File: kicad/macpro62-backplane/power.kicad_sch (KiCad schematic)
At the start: 0 parts

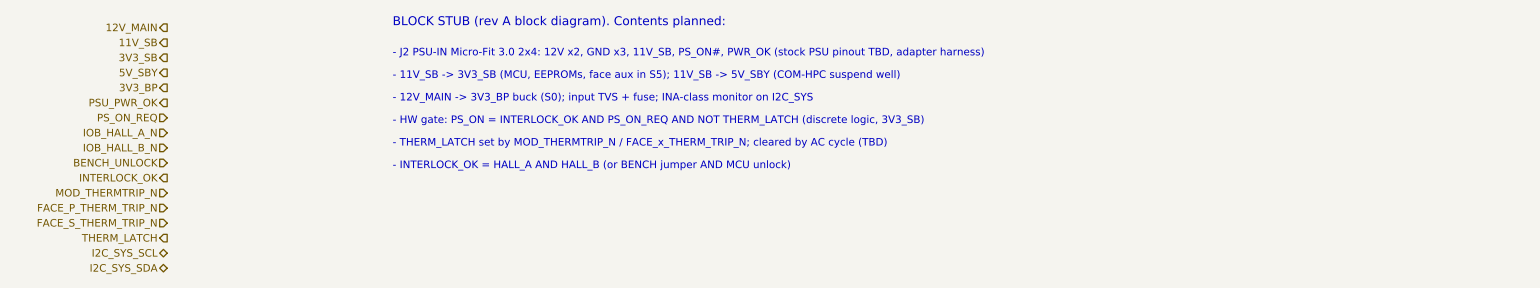
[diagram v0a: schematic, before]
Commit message: Cross-board compatibility audit: interface control doc, CR-BP-1 applied, J2/J3 row-swap pinouts, 15-pin face AUX, fan header removed from backplane, CPU board i226/BT1 cleanup
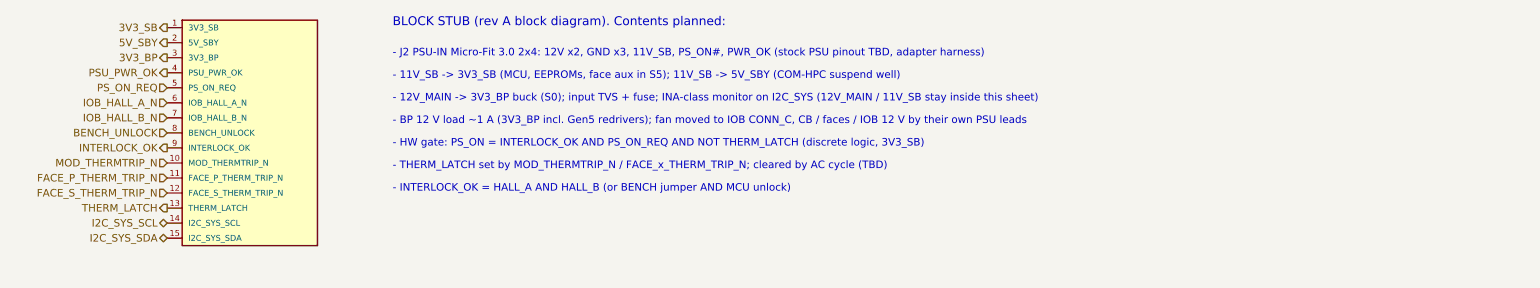
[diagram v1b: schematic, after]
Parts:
- added #BLK1: STUB_POWER, symbol MP62:STUB_POWER
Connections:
- net 3V3_BP: now also #BLK1.3 (3V3_BP)
- net 3V3_SB: now also #BLK1.1 (3V3_SB)
- net 5V_SBY: now also #BLK1.2 (5V_SBY)
- net BENCH_UNLOCK: now also #BLK1.8 (BENCH_UNLOCK)
- net FACE_P_THERM_TRIP_N: now also #BLK1.11 (FACE_P_THERM_TRIP_N)
- net FACE_S_THERM_TRIP_N: now also #BLK1.12 (FACE_S_THERM_TRIP_N)
- net I2C_SYS_SCL: now also #BLK1.14 (I2C_SYS_SCL)
- net I2C_SYS_SDA: now also #BLK1.15 (I2C_SYS_SDA)
- net INTERLOCK_OK: now also #BLK1.9 (INTERLOCK_OK)
- net IOB_HALL_A_N: now also #BLK1.6 (IOB_HALL_A_N)
- net IOB_HALL_B_N: now also #BLK1.7 (IOB_HALL_B_N)
- net MOD_THERMTRIP_N: now also #BLK1.10 (MOD_THERMTRIP_N)
- net PSU_PWR_OK: now also #BLK1.4 (PSU_PWR_OK)
- net PS_ON_REQ: now also #BLK1.5 (PS_ON_REQ)
- net THERM_LATCH: now also #BLK1.13 (THERM_LATCH)
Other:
- note added: "- 12V_MAIN -> 3V3_BP buck (S0); input TVS + fuse; INA-class monitor on I2C_SYS (12V_MAIN / 11V_SB stay inside this sheet)"
- note added: "- BP 12 V load ~1 A (3V3_BP incl. Gen5 redrivers); fan moved to IOB CONN_C, CB / faces / IOB 12 V by their own PSU leads"
- note removed: "- 12V_MAIN -> 3V3_BP buck (S0); input TVS + fuse; INA-class monitor on I2C_SYS"
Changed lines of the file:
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@@
 	(title_block
 		(title "MP62 backplane: Power input, standby rails, safety gate")
-		(date "2026-10-01")
-		(rev "A-bd1")
-		(comment 1 "Block stub: hierarchical labels only, circuit TBD")
+		(date "2026-10-02")
+		(rev "A-bd2")
+		(comment 1 "Block stub: hierarchical labels + one non-BOM stub symbol (#BLKn, passive pins) so ERC sees the nets; circuit TBD")
 	)
-	(hierarchical_label "12V_MAIN"
+	(hierarchical_label "3V3_SB"
 		(shape output)
 		(at 38.1 30.48 180)
 		(effects (font (size 1.27 1.27)) (justify right))
 	)
-	(hierarchical_label "11V_SB"
+	(hierarchical_label "5V_SBY"
 		(shape output)
 		(at 38.1 33.02 180)
 		(effects (font (size 1.27 1.27)) (justify right))
 	)
-	(hierarchical_label "3V3_SB"
+	(hierarchical_label "3V3_BP"
 		(shape output)
 		(at 38.1 35.56 180)
 		(effects (font (size 1.27 1.27)) (justify right))
 	)
-	(hierarchical_label "5V_SBY"
+	(hierarchical_label "PSU_PWR_OK"
 		(shape output)
 		(at 38.1 38.10 180)
 		(effects (font (size 1.27 1.27)) (justify right))
 	)
-	(hierarchical_label "3V3_BP"
-		(shape output)
+	(hierarchical_label "PS_ON_REQ"
+		(shape input)
 		(at 38.1 40.64 180)
 		(effects (font (size 1.27 1.27)) (justify right))
 	)
-	(hierarchical_label "PSU_PWR_OK"
-		(shape output)
+	(hierarchical_label "IOB_HALL_A_N"
+		(shape input)
 		(at 38.1 43.18 180)
 		(effects (font (size 1.27 1.27)) (justify right))
 	)
-	(hierarchical_label "PS_ON_REQ"
+	(hierarchical_label "IOB_HALL_B_N"
 		(shape input)
 		(at 38.1 45.72 180)
 		(effects (font (size 1.27 1.27)) (justify right))
 	)
-	(hierarchical_label "IOB_HALL_A_N"
+	(hierarchical_label "BENCH_UNLOCK"
 		(shape input)
 		(at 38.1 48.26 180)
 		(effects (font (size 1.27 1.27)) (justify right))
 	)
-	(hierarchical_label "IOB_HALL_B_N"
-		(shape input)
+	(hierarchical_label "INTERLOCK_OK"
+		(shape output)
 		(at 38.1 50.80 180)
 		(effects (font (size 1.27 1.27)) (justify right))
 	)
-	(hierarchical_label "BENCH_UNLOCK"
+	(hierarchical_label "MOD_THERMTRIP_N"
 		(shape input)
 		(at 38.1 53.34 180)
 		(effects (font (size 1.27 1.27)) (justify right))
 	)
-	(hierarchical_label "INTERLOCK_OK"
-		(shape output)
+	(hierarchical_label "FACE_P_THERM_TRIP_N"
+		(shape input)
 		(at 38.1 55.88 180)
 		(effects (font (size 1.27 1.27)) (justify right))
 	)
-	(hierarchical_label "MOD_THERMTRIP_N"
+	(hierarchical_label "FACE_S_THERM_TRIP_N"
 		(shape input)
 		(at 38.1 58.42 180)
 		(effects (font (size 1.27 1.27)) (justify right))
 	)
-	(hierarchical_label "FACE_P_THERM_TRIP_N"
-		(shape input)
-		(at 38.1 60.96 180)
-		(effects (font (size 1.27 1.27)) (justify right))
-	)
-	(hierarchical_label "FACE_S_THERM_TRIP_N"
-		(shape input)
-		(at 38.1 63.50 180)
-		(effects (font (size 1.27 1.27)) (justify right))
-	)
 	(hierarchical_label "THERM_LATCH"
 		(shape output)
-		(at 38.1 66.04 180)
+		(at 38.1 60.96 180)
 		(effects (font (size 1.27 1.27)) (justify right))
 	)
 	(hierarchical_label "I2C_SYS_SCL"
 		(shape bidirectional)
-		(at 38.1 68.58 180)
+		(at 38.1 63.50 180)
 		(effects (font (size 1.27 1.27)) (justify right))
 	)
 	(hierarchical_label "I2C_SYS_SDA"
 		(shape bidirectional)
-		(at 38.1 71.12 180)
+		(at 38.1 66.04 180)
 		(effects (font (size 1.27 1.27)) (justify right))
+	)
+	(symbol
+		(lib_id "MP62:STUB_POWER")
+		(at 38.1 30.48 0)
+		(unit 1)
+		(exclude_from_sim yes)
+		(in_bom no)
+		(on_board no)
+		(dnp no)
+		(property "Reference" "#BLK1"
+			(at 40.64 27.94 0)
+			(effects (font (size 1.27 1.27)) (justify left) (hide yes))
+		)
+		(property "Value" "STUB_POWER"
+			(at 40.64 26.67 0)
+			(effects (font (size 1.27 1.27)) (justify left) (hide yes))
+		)
+		(pin "1"
+		)
+		(pin "2"
+		)
+		(pin "3"
+		)
+		(pin "4"
+		)
+		(pin "5"
+		)
+		(pin "6"
+		)
+		(pin "7"
+		)
+		(pin "8"
+		)
+		(pin "9"
+		)
+		(pin "10"
+		)
+		(pin "11"
+		)
+		(pin "12"
+		)
+		(pin "13"
+		)
+		(pin "14"
+		)
+		(pin "15"
+		)
+		(instances
+			(project "backplane"
+				(path "/6a1c2d3e-0000-4000-8000-000000000062/a332e25f-e9d1-49f2-91b1-ad3b48f5f406"
+					(reference "#BLK1")
+					(unit 1)
+				)
+			)
+		)
 	)
 	(text "BLOCK STUB (rev A block diagram). Contents planned:"
@@
 		(effects (font (size 1.27 1.27)) (justify left bottom))
 	)
-	(text "- 12V_MAIN -> 3V3_BP buck (S0); input TVS + fuse; INA-class monitor on I2C_SYS"
+	(text "- 12V_MAIN -> 3V3_BP buck (S0); input TVS + fuse; INA-class monitor on I2C_SYS (12V_MAIN / 11V_SB stay inside this sheet)"
 		(exclude_from_sim no)
 		(at 76.20 43.18 0)
 		(effects (font (size 1.27 1.27)) (justify left bottom))
 	)
-	(text "- HW gate: PS_ON = INTERLOCK_OK AND PS_ON_REQ AND NOT THERM_LATCH (discrete logic, 3V3_SB)"
+	(text "- BP 12 V load ~1 A (3V3_BP incl. Gen5 redrivers); fan moved to IOB CONN_C, CB / faces / IOB 12 V by their own PSU leads"
 		(exclude_from_sim no)
 		(at 76.20 46.99 0)
 		(effects (font (size 1.27 1.27)) (justify left bottom))
 	)
-	(text "- THERM_LATCH set by MOD_THERMTRIP_N / FACE_x_THERM_TRIP_N; cleared by AC cycle (TBD)"
+	(text "- HW gate: PS_ON = INTERLOCK_OK AND PS_ON_REQ AND NOT THERM_LATCH (discrete logic, 3V3_SB)"
 		(exclude_from_sim no)
 		(at 76.20 50.80 0)
 		(effects (font (size 1.27 1.27)) (justify left bottom))
 	)
-	(text "- INTERLOCK_OK = HALL_A AND HALL_B (or BENCH jumper AND MCU unlock)"
+	(text "- THERM_LATCH set by MOD_THERMTRIP_N / FACE_x_THERM_TRIP_N; cleared by AC cycle (TBD)"
 		(exclude_from_sim no)
 		(at 76.20 54.61 0)
 		(effects (font (size 1.27 1.27)) (justify left bottom))
 	)
+	(text "- INTERLOCK_OK = HALL_A AND HALL_B (or BENCH jumper AND MCU unlock)"
+		(exclude_from_sim no)
+		(at 76.20 58.42 0)
+		(effects (font (size 1.27 1.27)) (justify left bottom))
+	)

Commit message: ICD rev 2: 45 deg faces, 445 W ceiling + live power target (INA228 telemetry), ribbon MCIO jog cables, BT on S0, fan fail-safe, port-module I2C map
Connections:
- new net PWR_ALERT_BP_N: #BLK1.16 (PWR_ALERT_BP_N)
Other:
- note added: "- 12V_MAIN -> 3V3_BP buck (S0); input TVS + fuse; INA228 power monitor 0x40 on I2C_SYS, ALERT -> PWR_ALERT_BP_N (12V_MAIN / 11V_SB stay inside this sheet)"
- note removed: "- 12V_MAIN -> 3V3_BP buck (S0); input TVS + fuse; INA-class monitor on I2C_SYS (12V_MAIN / 11V_SB stay inside this sheet)"
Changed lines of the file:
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@@
+		(effects (font (size 1.27 1.27)) (justify right))
+	)
+	(hierarchical_label "PWR_ALERT_BP_N"
+		(shape output)
+		(at 38.1 68.58 180)
 		(effects (font (size 1.27 1.27)) (justify right))
 	)
@@
 		(pin "15"
 		)
+		(pin "16"
+		)
 		(instances
 			(project "backplane"
-				(path "/6a1c2d3e-0000-4000-8000-000000000062/a332e25f-e9d1-49f2-91b1-ad3b48f5f406"
+				(path "/6a1c2d3e-0000-4000-8000-000000000062/aab28876-f196-4be9-929d-8b71f5b119f9"
 					(reference "#BLK1")
 					(unit 1)
@@
 		(effects (font (size 1.27 1.27)) (justify left bottom))
 	)
-	(text "- 12V_MAIN -> 3V3_BP buck (S0); input TVS + fuse; INA-class monitor on I2C_SYS (12V_MAIN / 11V_SB stay inside this sheet)"
+	(text "- 12V_MAIN -> 3V3_BP buck (S0); input TVS + fuse; INA228 power monitor 0x40 on I2C_SYS, ALERT -> PWR_ALERT_BP_N (12V_MAIN / 11V_SB stay inside this sheet)"
 		(exclude_from_sim no)
 		(at 76.20 43.18 0)
